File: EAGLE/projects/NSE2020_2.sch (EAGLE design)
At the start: 14 parts

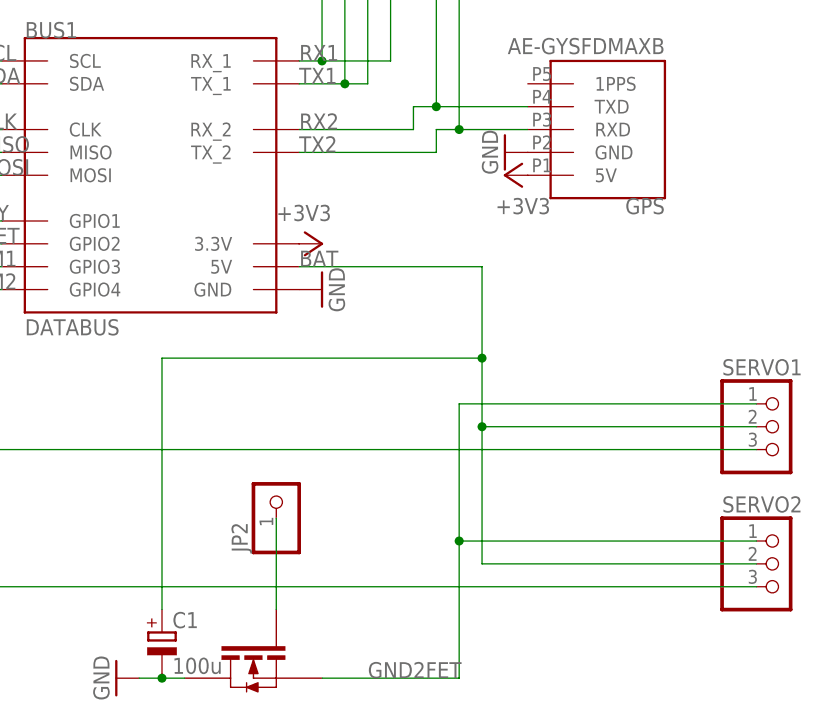
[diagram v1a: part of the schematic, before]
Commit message: 第2次試作で見つかったミスの修正
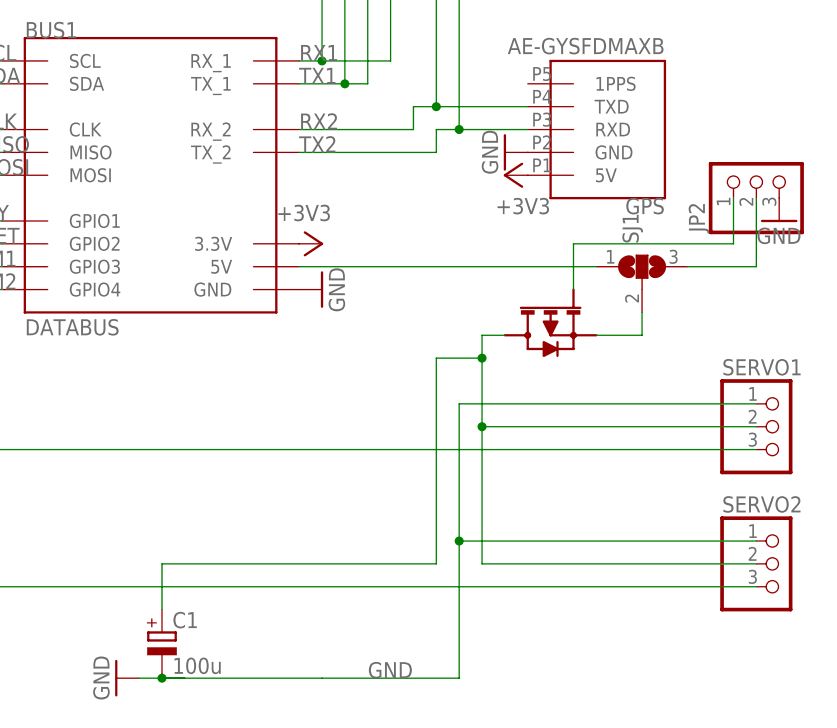
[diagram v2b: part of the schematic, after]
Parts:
- removed FET1: 2SK4033, 2SK4033:2SK4033
- added SJ1: (no value), jumper:SJ2W
- added U$1: 2SJ681, 2SJ681:2SJ681
- JP2: device pinhead:PINHD-1X1 -> pinhead:PINHD-1X3
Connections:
- removed net GND2FET: FET1.S, SERVO1.1, SERVO2.1
- removed net SERVO_GATE: FET1.G, JP2.1
- new net 5V_CELL: BUS1.5V, SJ1.1
- new net BAT_CELL: JP2.2, SJ1.3
- new net N$1: SJ1.2, U$1.P$3
- new net N$2: JP2.1, U$1.P$2
- net BAT: now also U$1.P$1; no longer BUS1.5V
- net GND: now also JP2.3, SERVO1.1, SERVO2.1; no longer FET1.D
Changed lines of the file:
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@@
 <part name="SERVO1" library="pinhead" library_urn="urn:adsk.eagle:library:325" deviceset="PINHD-1X3" device="" package3d_urn="urn:adsk.eagle:package:22458/2"/>
 <part name="SERVO2" library="pinhead" library_urn="urn:adsk.eagle:library:325" deviceset="PINHD-1X3" device="" package3d_urn="urn:adsk.eagle:package:22458/2"/>
-<part name="FET1" library="2SK4033" deviceset="2SK4033" device=""/>
 <part name="GND6" library="supply1" library_urn="urn:adsk.eagle:library:371" deviceset="GND" device=""/>
 <part name="BUS2" library="databus" deviceset="DATABUS" device=""/>
@@
 <part name="R2" library="rcl" library_urn="urn:adsk.eagle:library:334" deviceset="R-EU_" device="R2012" package3d_urn="urn:adsk.eagle:package:23543/2" value="330"/>
 <part name="ANT1" library="IM920ANT-XS" deviceset="IM920ANT-XS" device=""/>
-<part name="JP2" library="pinhead" library_urn="urn:adsk.eagle:library:325" deviceset="PINHD-1X1" device="" package3d_urn="urn:adsk.eagle:package:22485/2"/>
 <part name="C1" library="rcl" library_urn="urn:adsk.eagle:library:334" deviceset="CPOL-EU" device="E2.5-6" package3d_urn="urn:adsk.eagle:package:23349/1" value="100u"/>
+<part name="U$1" library="2SJ681" deviceset="2SJ681" device=""/>
+<part name="SJ1" library="jumper" library_urn="urn:adsk.eagle:library:252" deviceset="SJ2W" device="" package3d_urn="urn:adsk.eagle:package:15474/1"/>
+<part name="JP2" library="pinhead" library_urn="urn:adsk.eagle:library:325" deviceset="PINHD-1X3" device="" package3d_urn="urn:adsk.eagle:package:22458/2"/>
+<part name="GND9" library="supply1" library_urn="urn:adsk.eagle:library:371" deviceset="GND" device=""/>
 </parts>
 <sheets>
@@
 <attribute name="VALUE" x="156.21" y="-17.78" size="1.778" layer="96"/>
 </instance>
-<instance part="FET1" gate="G$1" x="104.14" y="-20.32" smashed="yes" rot="MR0"/>
 <instance part="GND6" gate="1" x="88.9" y="-22.86" smashed="yes" rot="R270">
 <attribute name="VALUE" x="86.36" y="-20.32" size="1.778" layer="96" rot="R270"/>
@@
 </instance>
 <instance part="ANT1" gate="G$1" x="27.94" y="66.04" smashed="yes"/>
-<instance part="JP2" gate="G$1" x="106.68" y="-2.54" smashed="yes" rot="R90">
-<attribute name="NAME" x="103.505" y="-8.89" size="1.778" layer="95" rot="R90"/>
-<attribute name="VALUE" x="111.76" y="-8.89" size="1.778" layer="96" rot="R90"/>
-</instance>
 <instance part="C1" gate="G$1" x="93.98" y="-17.78" smashed="yes">
 <attribute name="NAME" x="95.123" y="-17.2974" size="1.778" layer="95"/>
 <attribute name="VALUE" x="95.123" y="-22.3774" size="1.778" layer="96"/>
+</instance>
+<instance part="U$1" gate="G$1" x="137.16" y="15.24" smashed="yes" rot="MR180"/>
+<instance part="SJ1" gate="G$1" x="147.32" y="22.86" smashed="yes" rot="R90">
+<attribute name="NAME" x="146.939" y="25.4" size="1.778" layer="95" rot="R90"/>
+<attribute name="VALUE" x="149.225" y="25.4" size="1.778" layer="96" rot="R90"/>
+</instance>
+<instance part="JP2" gate="A" x="160.02" y="33.02" smashed="yes" rot="R90">
+<attribute name="NAME" x="154.305" y="26.67" size="1.778" layer="95" rot="R90"/>
+<attribute name="VALUE" x="167.64" y="26.67" size="1.778" layer="96" rot="R90"/>
+</instance>
+<instance part="GND9" gate="1" x="162.56" y="27.94" smashed="yes">
+<attribute name="VALUE" x="160.02" y="25.4" size="1.778" layer="96"/>
 </instance>
 </instances>
@@
 </segment>
 <segment>
-<pinref part="FET1" gate="G$1" pin="D"/>
 <pinref part="GND6" gate="1" pin="GND"/>
 <wire x1="96.52" y1="-22.86" x2="93.98" y2="-22.86" width="0.1524" layer="91"/>
@@
 <wire x1="93.98" y1="-22.86" x2="91.44" y2="-22.86" width="0.1524" layer="91"/>
 <junction x="93.98" y="-22.86"/>
+<pinref part="SERVO2" gate="A" pin="1"/>
+<pinref part="SERVO1" gate="A" pin="1"/>
+<wire x1="160.02" y1="7.62" x2="127" y2="7.62" width="0.1524" layer="91"/>
+<wire x1="127" y1="7.62" x2="127" y2="-7.62" width="0.1524" layer="91"/>
+<wire x1="127" y1="-7.62" x2="127" y2="-22.86" width="0.1524" layer="91"/>
+<wire x1="127" y1="-22.86" x2="111.76" y2="-22.86" width="0.1524" layer="91"/>
+<wire x1="160.02" y1="-7.62" x2="127" y2="-7.62" width="0.1524" layer="91"/>
+<junction x="127" y="-7.62"/>
+<label x="116.84" y="-22.86" size="1.778" layer="95"/>
+<wire x1="93.98" y1="-22.86" x2="111.76" y2="-22.86" width="0.1524" layer="91"/>
 </segment>
 <segment>
@@
 <pinref part="JP1" gate="A" pin="3"/>
 <wire x1="17.78" y1="96.52" x2="20.32" y2="96.52" width="0.1524" layer="91"/>
+</segment>
+<segment>
+<pinref part="JP2" gate="A" pin="3"/>
+<pinref part="GND9" gate="1" pin="GND"/>
 </segment>
 </net>
@@
 <segment>
 <pinref part="SERVO1" gate="A" pin="2"/>
-<wire x1="109.22" y1="22.86" x2="129.54" y2="22.86" width="0.1524" layer="91"/>
-<wire x1="129.54" y1="22.86" x2="129.54" y2="12.7" width="0.1524" layer="91"/>
+<wire x1="129.54" y1="15.24" x2="129.54" y2="12.7" width="0.1524" layer="91"/>
 <wire x1="129.54" y1="12.7" x2="129.54" y2="5.08" width="0.1524" layer="91"/>
 <wire x1="129.54" y1="5.08" x2="160.02" y2="5.08" width="0.1524" layer="91"/>
@@
 <wire x1="129.54" y1="-10.16" x2="160.02" y2="-10.16" width="0.1524" layer="91"/>
 <junction x="129.54" y="5.08"/>
-<label x="109.22" y="22.86" size="1.778" layer="95"/>
-<pinref part="BUS1" gate="G$1" pin="5V"/>
 <pinref part="C1" gate="G$1" pin="+"/>
-<wire x1="93.98" y1="-15.24" x2="93.98" y2="12.7" width="0.1524" layer="91"/>
-<wire x1="93.98" y1="12.7" x2="129.54" y2="12.7" width="0.1524" layer="91"/>
+<wire x1="93.98" y1="-15.24" x2="93.98" y2="-10.16" width="0.1524" layer="91"/>
 <junction x="129.54" y="12.7"/>
+<wire x1="124.46" y1="12.7" x2="129.54" y2="12.7" width="0.1524" layer="91"/>
+<wire x1="132.08" y1="15.24" x2="129.54" y2="15.24" width="0.1524" layer="91"/>
+<pinref part="U$1" gate="G$1" pin="P$1"/>
+<wire x1="93.98" y1="-10.16" x2="124.46" y2="-10.16" width="0.1524" layer="91"/>
+<wire x1="124.46" y1="-10.16" x2="124.46" y2="12.7" width="0.1524" layer="91"/>
 </segment>
 <segment>
@@
 <wire x1="109.22" y1="71.12" x2="111.76" y2="71.12" width="0.1524" layer="91"/>
 <label x="109.22" y="71.12" size="1.778" layer="95"/>
-</segment>
-</net>
-<net name="GND2FET" class="1">
-<segment>
-<pinref part="SERVO2" gate="A" pin="1"/>
-<pinref part="SERVO1" gate="A" pin="1"/>
-<wire x1="160.02" y1="7.62" x2="127" y2="7.62" width="0.1524" layer="91"/>
-<pinref part="FET1" gate="G$1" pin="S"/>
-<wire x1="127" y1="7.62" x2="127" y2="-7.62" width="0.1524" layer="91"/>
-<wire x1="127" y1="-7.62" x2="127" y2="-22.86" width="0.1524" layer="91"/>
-<wire x1="127" y1="-22.86" x2="111.76" y2="-22.86" width="0.1524" layer="91"/>
-<wire x1="160.02" y1="-7.62" x2="127" y2="-7.62" width="0.1524" layer="91"/>
-<junction x="127" y="-7.62"/>
-<label x="116.84" y="-22.86" size="1.778" layer="95"/>
 </segment>
 </net>
@@
 </segment>
 </net>
-<net name="SERVO_GATE" class="3">
-<segment>
-<pinref part="JP2" gate="G$1" pin="1"/>
-<pinref part="FET1" gate="G$1" pin="G"/>
-<wire x1="106.68" y1="-5.08" x2="106.68" y2="-15.24" width="0.1524" layer="91"/>
-</segment>
-</net>
+<net name="N$1" class="2">
+<segment>
+<pinref part="U$1" gate="G$1" pin="P$3"/>
+<wire x1="142.24" y1="15.24" x2="147.32" y2="15.24" width="0.1524" layer="91"/>
+<wire x1="147.32" y1="15.24" x2="147.32" y2="17.78" width="0.1524" layer="91"/>
+<pinref part="SJ1" gate="G$1" pin="2"/>
+</segment>
+</net>
+<net name="5V_CELL" class="2">
+<segment>
+<pinref part="BUS1" gate="G$1" pin="5V"/>
+<pinref part="SJ1" gate="G$1" pin="1"/>
+<wire x1="109.22" y1="22.86" x2="142.24" y2="22.86" width="0.1524" layer="91"/>
+</segment>
+</net>
+<net name="N$2" class="0">
+<segment>
+<pinref part="U$1" gate="G$1" pin="P$2"/>
+<wire x1="157.48" y1="25.4" x2="139.7" y2="25.4" width="0.1524" layer="91"/>
+<wire x1="139.7" y1="25.4" x2="139.7" y2="20.32" width="0.1524" layer="91"/>
+<pinref part="JP2" gate="A" pin="1"/>
+<wire x1="157.48" y1="25.4" x2="157.48" y2="30.48" width="0.1524" layer="91"/>
+</segment>
+</net>
+<net name="BAT_CELL" class="2">
+<segment>
+<pinref part="SJ1" gate="G$1" pin="3"/>
+<wire x1="152.4" y1="22.86" x2="160.02" y2="22.86" width="0.1524" layer="91"/>
+<wire x1="160.02" y1="22.86" x2="160.02" y2="30.48" width="0.1524" layer="91"/>
+<pinref part="JP2" gate="A" pin="2"/>
+</segment>
+</net>
